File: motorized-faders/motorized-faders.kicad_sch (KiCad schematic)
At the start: 46 parts, among them U1 MCP3208, U2 TB6612FNG, U4 TB6612FNG

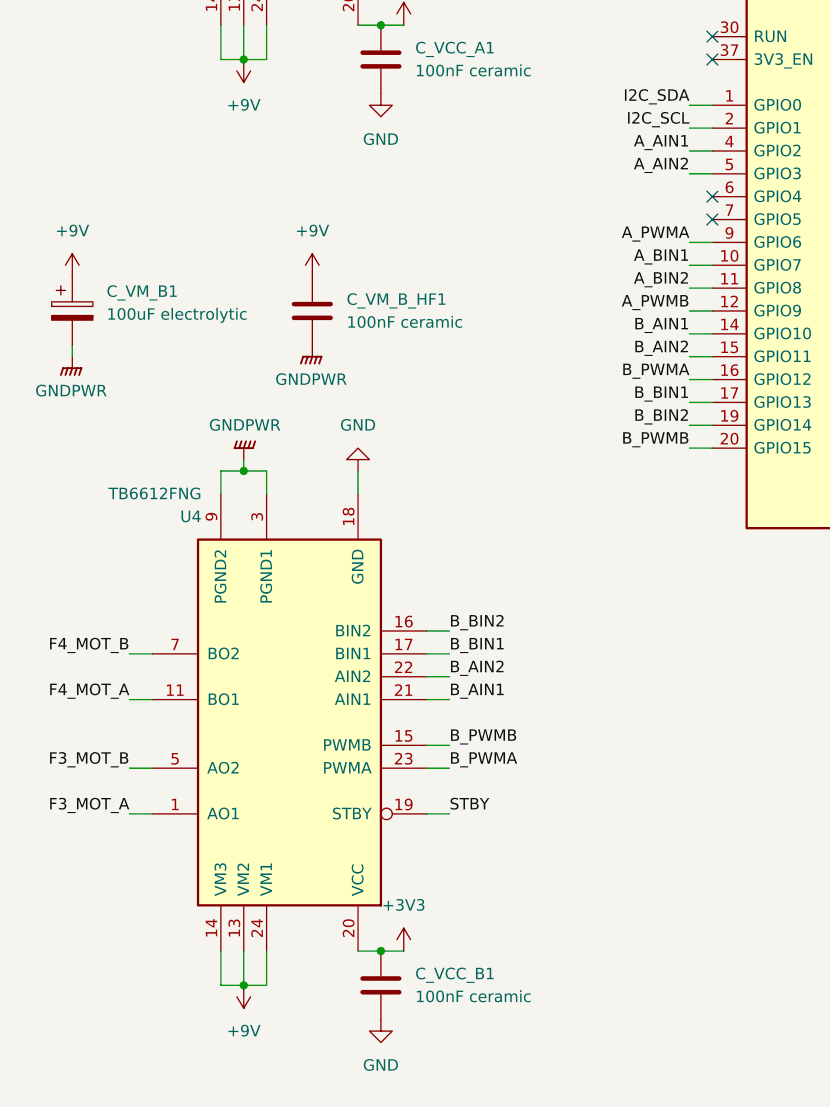
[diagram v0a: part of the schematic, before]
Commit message: kicad: assign all footprints
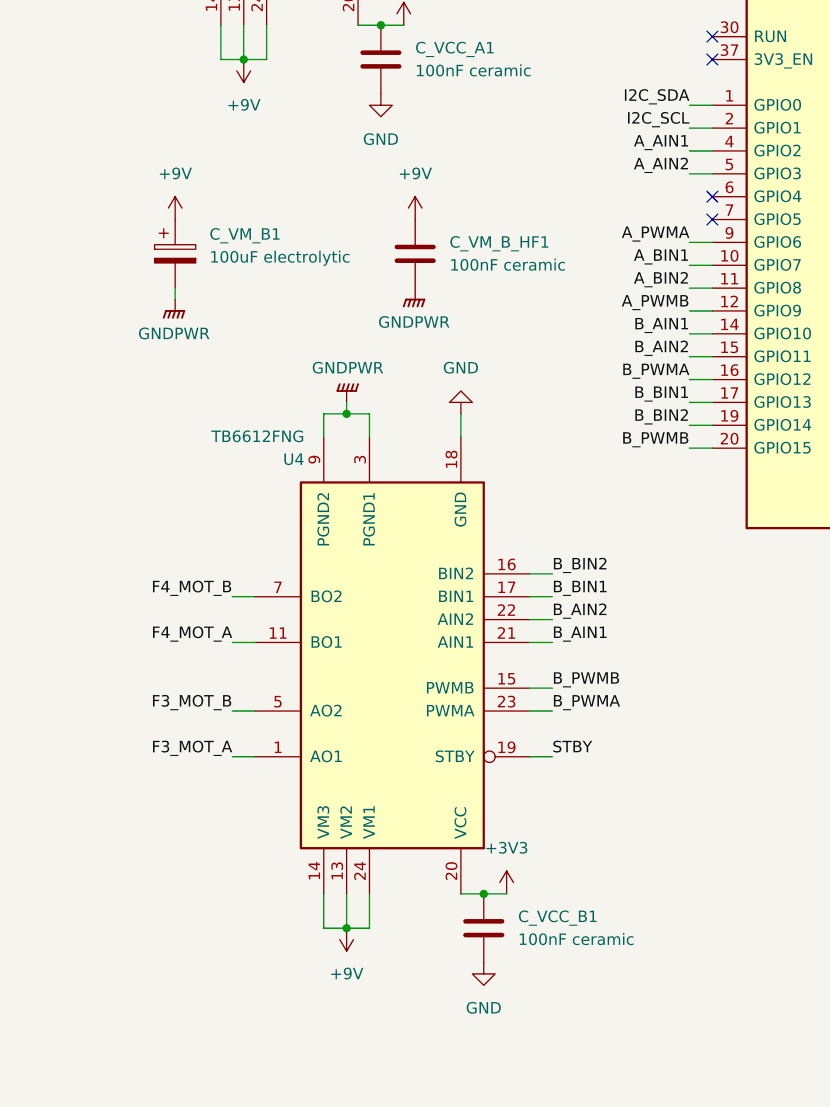
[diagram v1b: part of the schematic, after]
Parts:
- C_BTN_FADER1, C_BTN_GEN1, C_DISP_RES1, C_F1_WIPER1, C_F2_WIPER1, C_F3_WIPER1, C_F4_WIPER1, C_MCP3208_VDD_GND1, C_MCP3208_VREF_GND1, C_VCC_A1, C_VCC_B1, C_VM_A_HF1, C_VM_B_HF1: footprint (none) -> Capacitor_SMD:C_0805_2012Metric
- C_VM_A1, C_VM_B1: footprint (none) -> Capacitor_THT:CP_Radial_D8.0mm_P5.00mm
- J_PD1: footprint Package_DFN_QFN:WDFN-10-1EP_3x3mm_P0.5mm_EP1.8x2.5mm -> Connector_PinHeader_2.54mm:PinHeader_1x04_P2.54mm_Vertical
- NT1: footprint Package_TO_SOT_SMD:TDSON-8-1 -> NetTie:NetTie-2_SMD_Pad2.0mm
- R_BTN_FADER1, R_BTN_GEN_PU1, R_SW_F2, R_SW_F3, R_SW_F4, R_SW_G2: footprint Package_QFP:LQFP-32_7x7mm_P0.8mm -> Resistor_SMD:R_0805_2012Metric
- R_DISP_RES1, R_F1_WIPER1, R_F2_WIPER1, R_F3_WIPER1, R_F4_WIPER1, R_VM_SENSE_BOT1, R_VM_SENSE_TOP1: footprint (none) -> Resistor_SMD:R_0805_2012Metric
- SW_F1, SW_F2, SW_F3, SW_F4, SW_G1, SW_G2: footprint Button_Switch_THT:SW_NKK_GW12LJP -> Button_Switch_THT:SW_SPST_Omron_B3F-40xx
- TP_3V3, TP_GND1: footprint Package_TO_SOT_SMD:SOT-23-5 -> TestPoint:TestPoint_THTPad_D1.5mm_Drill0.7mm
- TP_F1_ADC1, TP_GND2, TP_SCK1: footprint (none) -> TestPoint:TestPoint_THTPad_D1.5mm_Drill0.7mm
- TP_VM1: footprint Package_SO:TSSOP-16_4.4x5mm_P0.65mm -> TestPoint:TestPoint_THTPad_D1.5mm_Drill0.7mm
- U1: footprint (none) -> Package_DIP:DIP-16_W7.62mm
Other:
- moved on the sheet: C_VCC_B1, C_VM_B1, C_VM_B_HF1, U4

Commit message: pcb: header wiring not soldered, add mounting holes, place components
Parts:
- A1: footprint Module:RaspberryPi_Pico_Common_Unspecified -> Module:RaspberryPi_Pico_Common_THT
- SW_F1, SW_F2, SW_F3, SW_F4, SW_G1, SW_G2: footprint Button_Switch_THT:SW_SPST_Omron_B3F-40xx -> Connector_PinHeader_2.54mm:PinHeader_1x02_P2.54mm_Vertical
- renumbered U1 to U_ADC, U2 to U_MOT_A1, U4 to U_MOT_B1
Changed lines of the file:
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@@
 			)
 		)
-		(property "Footprint" "Button_Switch_THT:SW_SPST_Omron_B3F-40xx"
+		(property "Footprint" "Connector_PinHeader_2.54mm:PinHeader_1x02_P2.54mm_Vertical"
 			(at 207.01 104.14 0)
 			(hide yes)
@@
 			)
 		)
-		(property "Footprint" "Button_Switch_THT:SW_SPST_Omron_B3F-40xx"
+		(property "Footprint" "Connector_PinHeader_2.54mm:PinHeader_1x02_P2.54mm_Vertical"
 			(at 161.29 97.79 0)
 			(hide yes)
@@
 		(dnp no)
 		(fields_autoplaced yes)
-		(property "Reference" "U2"
-			(at 20.7167 44.45 0)
+		(property "Reference" "U_MOT_A1"
+			(at 41.2181 41.91 0)
 			(show_name no)
 			(do_not_autoplace no)
@@
 					(size 1.27 1.27)
 				)
-				(justify left)
+				(justify right)
 			)
 		)
 		(property "Value" "TB6612FNG"
-			(at 20.7167 41.91 0)
+			(at 41.2181 44.45 0)
 			(show_name no)
 			(do_not_autoplace no)
@@
 					(size 1.27 1.27)
 				)
-				(justify left)
+				(justify right)
 			)
 		)
@@
 			(project "motorized-faders"
 				(path "/b7e3fc1e-7c8d-4632-8bd7-928f8e22b8b2"
-					(reference "U2")
+					(reference "U_MOT_A1")
 					(unit 1)
 				)
@@
 			)
 		)
-		(property "Footprint" "Button_Switch_THT:SW_SPST_Omron_B3F-40xx"
+		(property "Footprint" "Connector_PinHeader_2.54mm:PinHeader_1x02_P2.54mm_Vertical"
 			(at 207.01 83.82 0)
 			(hide yes)
@@
 			)
 		)
-		(property "Footprint" "Button_Switch_THT:SW_SPST_Omron_B3F-40xx"
+		(property "Footprint" "Connector_PinHeader_2.54mm:PinHeader_1x02_P2.54mm_Vertical"
 			(at 207.01 114.3 0)
 			(hide yes)
@@
 		(dnp no)
 		(fields_autoplaced yes)
-		(property "Reference" "U4"
-			(at 32.1467 140.97 0)
+		(property "Reference" "U_MOT_B1"
+			(at 52.6481 138.43 0)
 			(show_name no)
 			(do_not_autoplace no)
@@
 					(size 1.27 1.27)
 				)
-				(justify left)
+				(justify right)
 			)
 		)
 		(property "Value" "TB6612FNG"
-			(at 32.1467 138.43 0)
+			(at 52.6481 140.97 0)
 			(show_name no)
 			(do_not_autoplace no)
@@
 					(size 1.27 1.27)
 				)
-				(justify left)
+				(justify right)
 			)
 		)
@@
 			(project "motorized-faders"
 				(path "/b7e3fc1e-7c8d-4632-8bd7-928f8e22b8b2"
-					(reference "U4")
+					(reference "U_MOT_B1")
 					(unit 1)
 				)
@@
 		(dnp no)
 		(fields_autoplaced yes)
-		(property "Reference" "U1"
+		(property "Reference" "U_ADC"
 			(at 268.5481 54.61 0)
 			(show_name no)
@@
 			(project "motorized-faders"
 				(path "/b7e3fc1e-7c8d-4632-8bd7-928f8e22b8b2"
-					(reference "U1")
+					(reference "U_ADC")
 					(unit 1)
 				)
@@
 			)
 		)
-		(property "Footprint" "Button_Switch_THT:SW_SPST_Omron_B3F-40xx"
+		(property "Footprint" "Connector_PinHeader_2.54mm:PinHeader_1x02_P2.54mm_Vertical"
 			(at 161.29 87.63 0)
 			(hide yes)
@@
 			)
 		)
-		(property "Footprint" "Button_Switch_THT:SW_SPST_Omron_B3F-40xx"
+		(property "Footprint" "Connector_PinHeader_2.54mm:PinHeader_1x02_P2.54mm_Vertical"
 			(at 207.01 93.98 0)
 			(hide yes)
@@
 			)
 		)
-		(property "Footprint" "Module:RaspberryPi_Pico_Common_Unspecified"
+		(property "Footprint" "Module:RaspberryPi_Pico_Common_THT"
 			(at 100.33 163.83 0)
 			(hide yes)

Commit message: pcb: grounds, first DRC errors fixed
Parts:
- renumbered U_ADC to U_ADC1
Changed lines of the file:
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@@
 		(dnp no)
 		(fields_autoplaced yes)
-		(property "Reference" "U_ADC"
+		(property "Reference" "U_ADC1"
 			(at 268.5481 54.61 0)
 			(show_name no)
@@
 			(project "motorized-faders"
 				(path "/b7e3fc1e-7c8d-4632-8bd7-928f8e22b8b2"
-					(reference "U_ADC")
+					(reference "U_ADC1")
 					(unit 1)
 				)

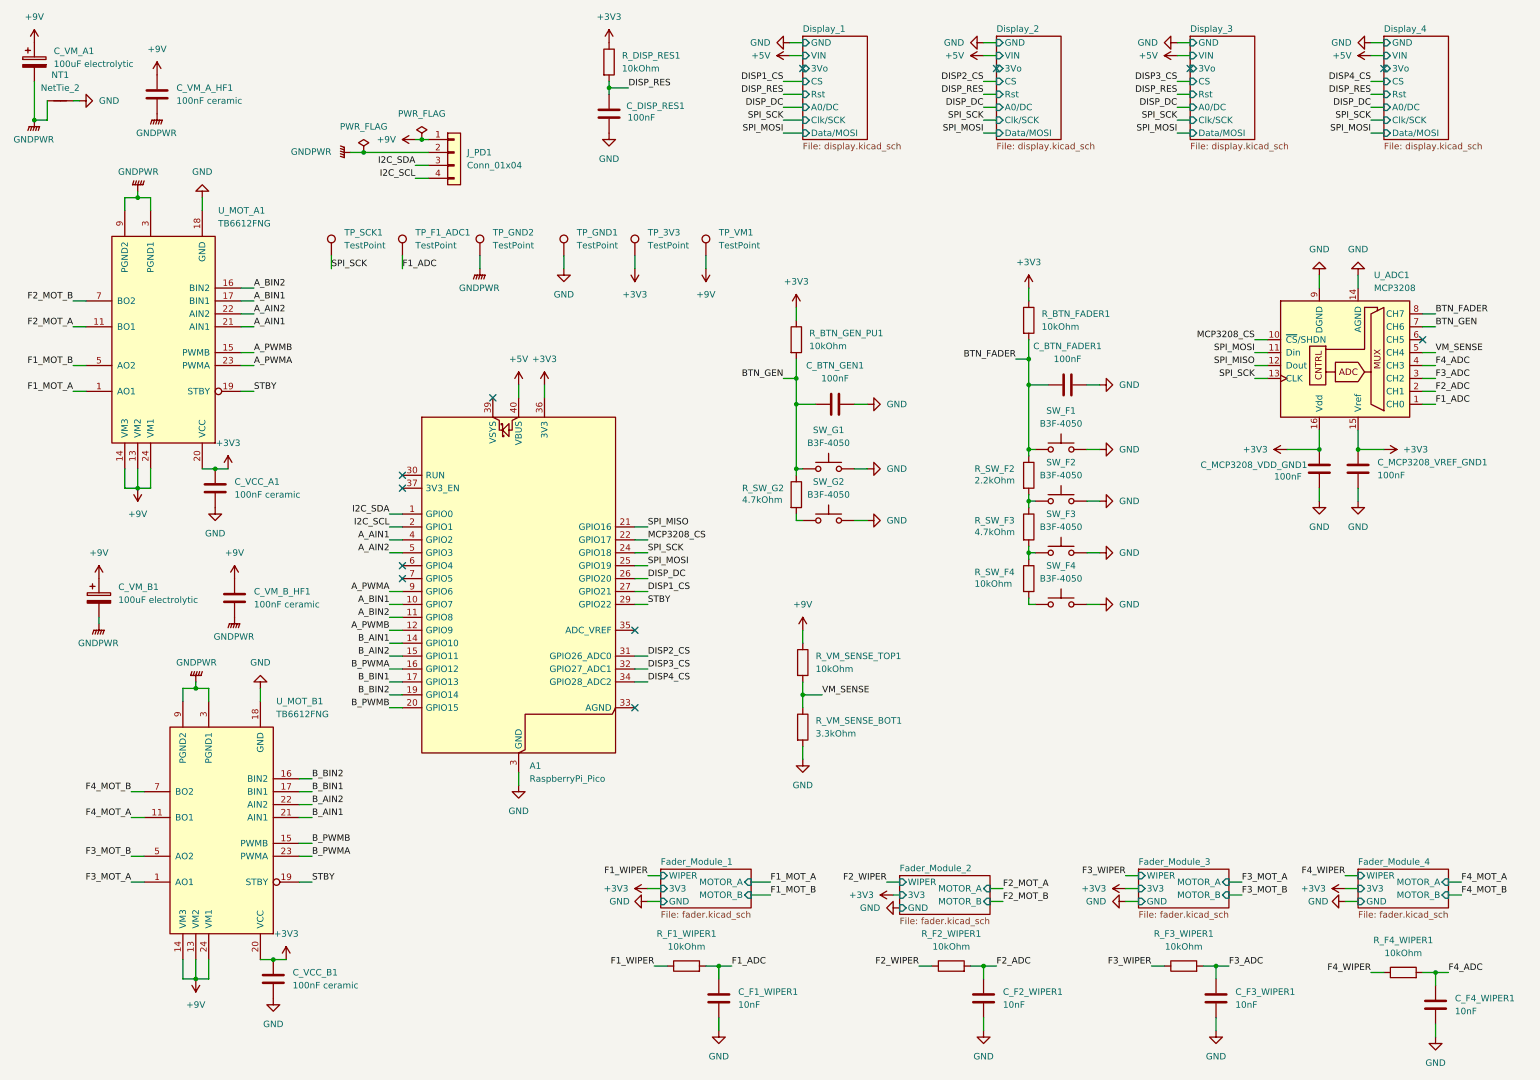
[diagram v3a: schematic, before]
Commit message: pcb: add TB6612 breakout headers, finish routing and grounds
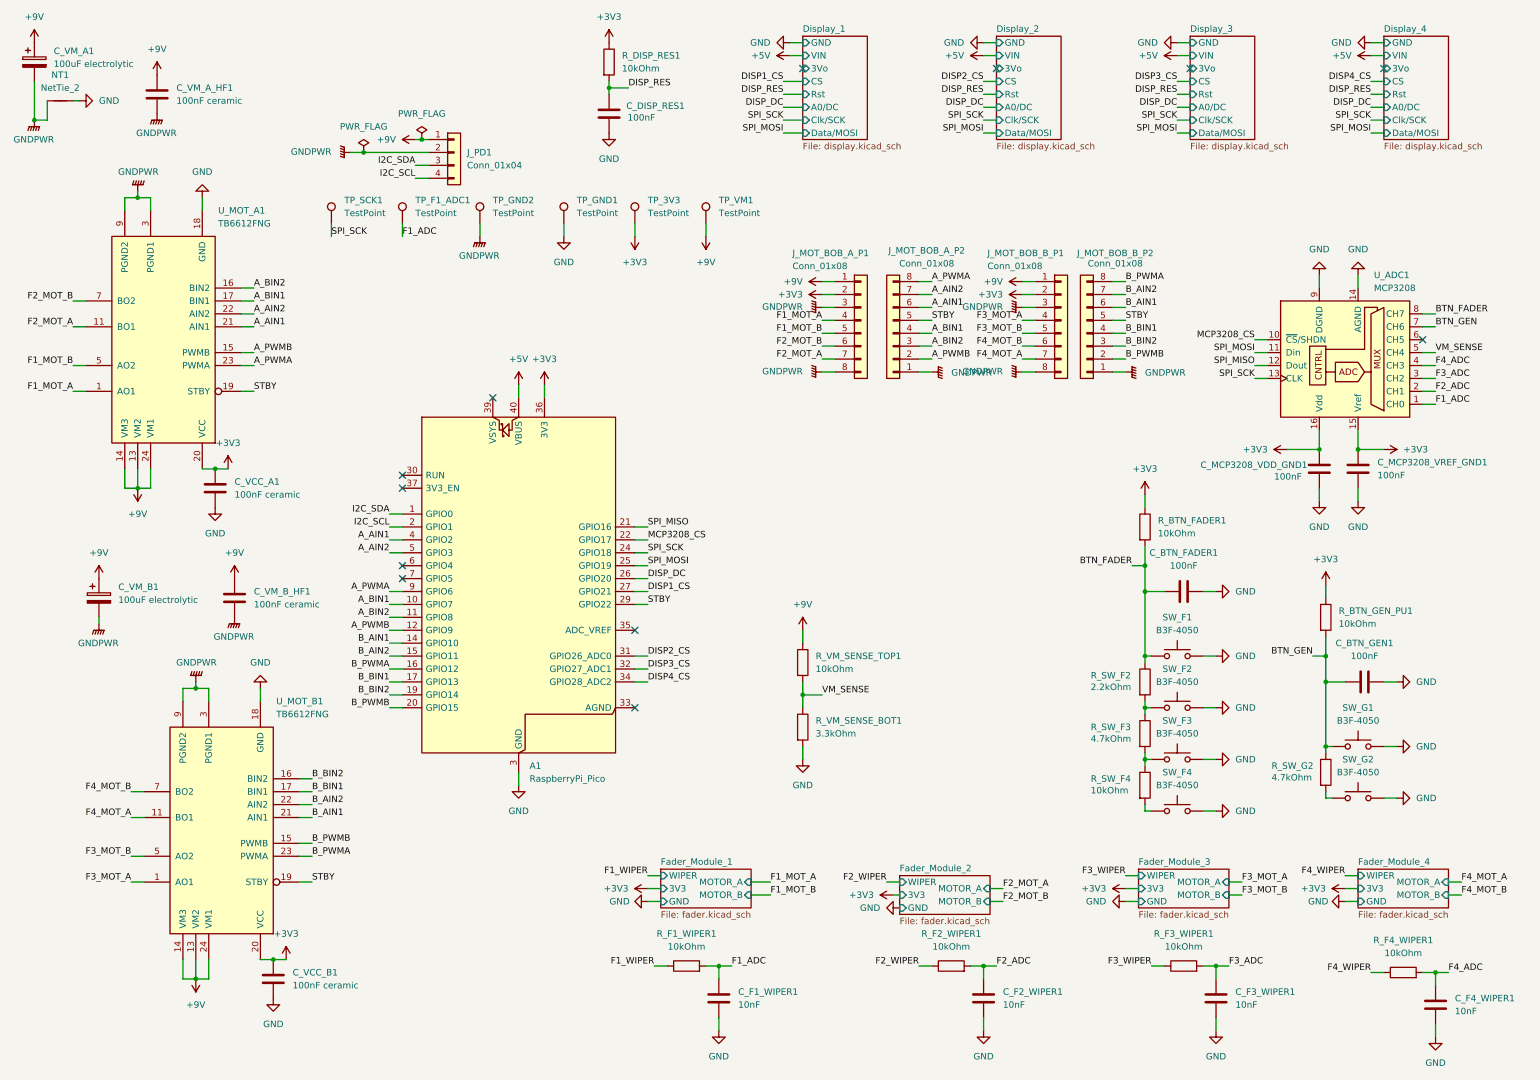
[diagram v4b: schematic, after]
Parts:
- added J_MOT_BOB_A_P1, J_MOT_BOB_A_P2, J_MOT_BOB_B_P1, J_MOT_BOB_B_P2: Conn_01x08, Connector_PinHeader_2.54mm:PinHeader_1x08_P2.54mm_Vertical, symbol Connector_Generic:Conn_01x08
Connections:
- net +3V3: now also J_MOT_BOB_A_P1.2 (Pin_2), J_MOT_BOB_B_P1.2 (Pin_2)
- net +9V: now also J_MOT_BOB_A_P1.1 (Pin_1), J_MOT_BOB_B_P1.1 (Pin_1)
- net A_AIN1: now also J_MOT_BOB_A_P2.6 (Pin_6)
- net A_AIN2: now also J_MOT_BOB_A_P2.7 (Pin_7)
- net A_BIN1: now also J_MOT_BOB_A_P2.4 (Pin_4)
- net A_BIN2: now also J_MOT_BOB_A_P2.3 (Pin_3)
- net A_PWMA: now also J_MOT_BOB_A_P2.8 (Pin_8)
- net A_PWMB: now also J_MOT_BOB_A_P2.2 (Pin_2)
- net B_AIN1: now also J_MOT_BOB_B_P2.6 (Pin_6)
- net B_AIN2: now also J_MOT_BOB_B_P2.7 (Pin_7)
- net B_BIN1: now also J_MOT_BOB_B_P2.4 (Pin_4)
- net B_BIN2: now also J_MOT_BOB_B_P2.3 (Pin_3)
- net B_PWMA: now also J_MOT_BOB_B_P2.8 (Pin_8)
- net B_PWMB: now also J_MOT_BOB_B_P2.2 (Pin_2)
- net F1_MOT_A: now also J_MOT_BOB_A_P1.4 (Pin_4)
- net F1_MOT_B: now also J_MOT_BOB_A_P1.5 (Pin_5)
- net F2_MOT_A: now also J_MOT_BOB_A_P1.7 (Pin_7)
- net F2_MOT_B: now also J_MOT_BOB_A_P1.6 (Pin_6)
- net F3_MOT_A: now also J_MOT_BOB_B_P1.4 (Pin_4)
- net F3_MOT_B: now also J_MOT_BOB_B_P1.5 (Pin_5)
- net F4_MOT_A: now also J_MOT_BOB_B_P1.7 (Pin_7)
- net F4_MOT_B: now also J_MOT_BOB_B_P1.6 (Pin_6)
- net GNDPWR: now also J_MOT_BOB_A_P1.3 (Pin_3), J_MOT_BOB_A_P1.8 (Pin_8), J_MOT_BOB_A_P2.1 (Pin_1), J_MOT_BOB_B_P1.3 (Pin_3), J_MOT_BOB_B_P1.8 (Pin_8), J_MOT_BOB_B_P2.1 (Pin_1)
- net STBY: now also J_MOT_BOB_A_P2.5 (Pin_5), J_MOT_BOB_B_P2.5 (Pin_5)
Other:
- moved on the sheet: C_BTN_FADER1, C_BTN_GEN1, R_BTN_FADER1, R_BTN_GEN_PU1, R_SW_F2, R_SW_F3, R_SW_F4, R_SW_G2, SW_F1, SW_F2, SW_F3, SW_F4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
